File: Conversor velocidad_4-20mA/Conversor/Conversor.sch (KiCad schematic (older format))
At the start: 24 parts, among them J1 Bornera Señal de Entrada, J2 Bornera continua > 15V, J3 BNC salida, Q1 BC848, U1 L7815, U2 4040, U3 4070, U4 TL082

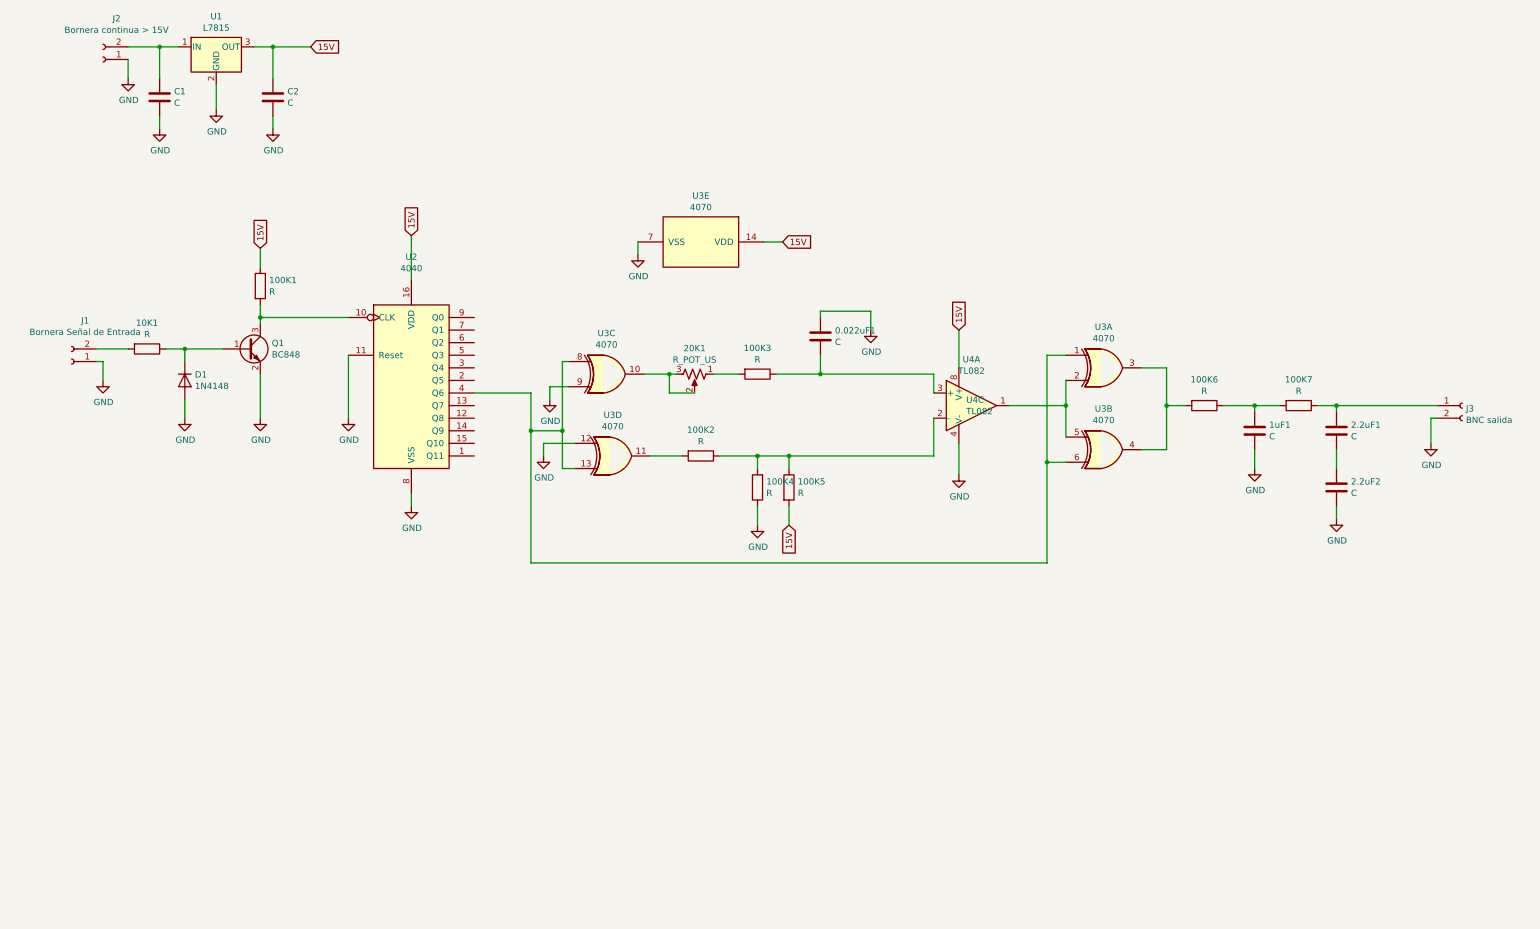
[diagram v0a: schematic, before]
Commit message: Esquemático final
Esquematico final con salida de 4-20mA
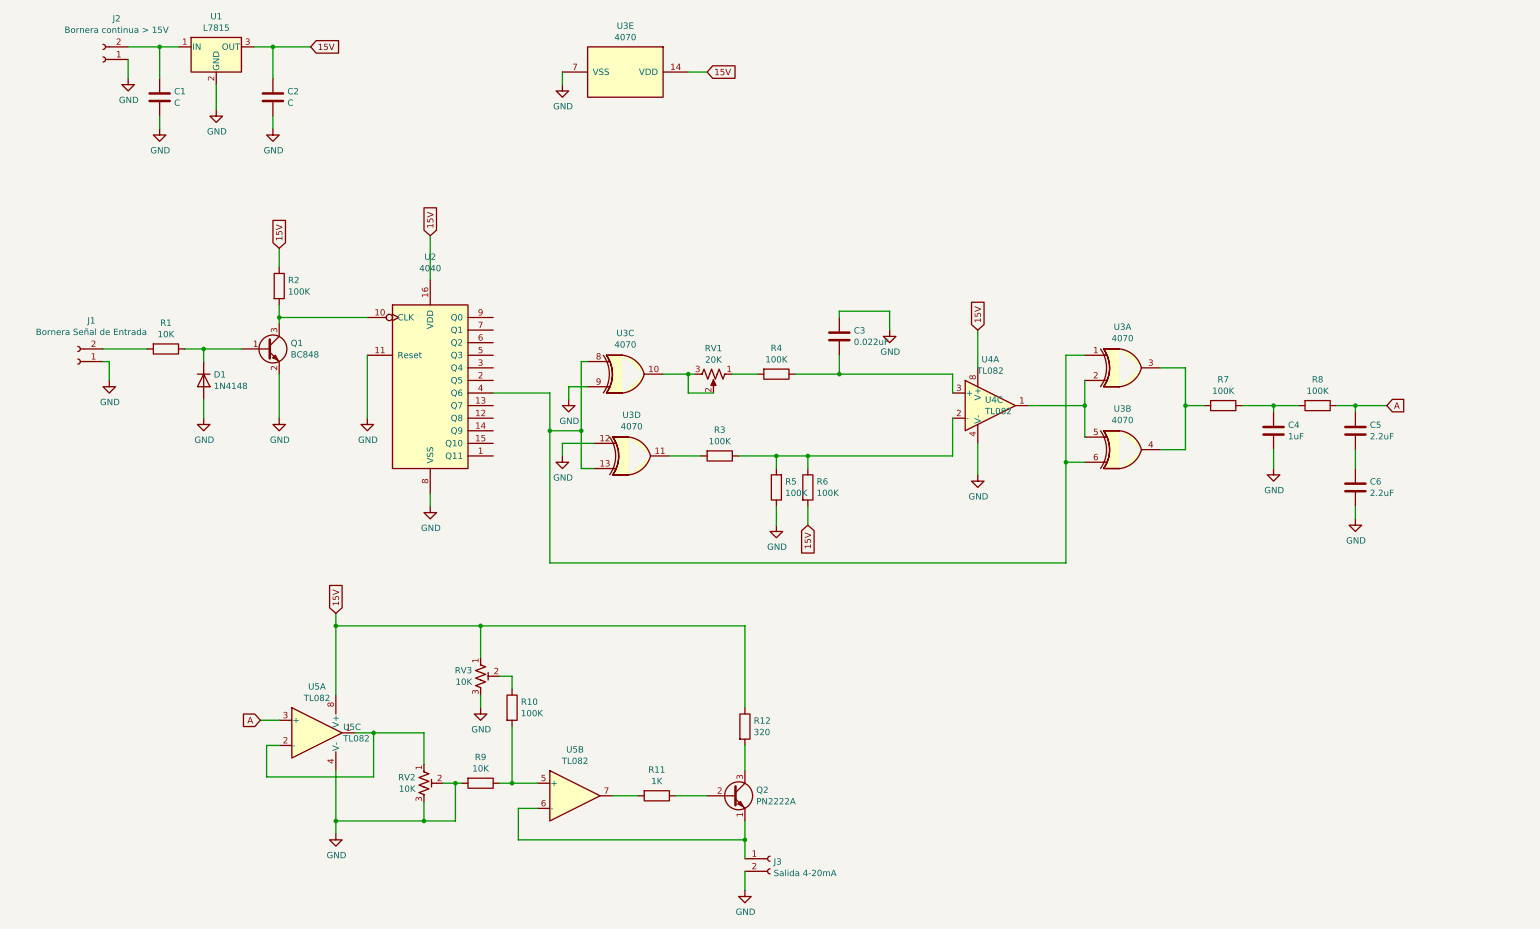
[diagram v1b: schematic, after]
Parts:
- added Q2: PN2222A, Package_TO_SOT_THT:TO-92_Inline, symbol Transistor_BJT:PN2222A
- added R10: 100K, symbol Device:R
- added R11: 1K, symbol Device:R
- added R12: 320, symbol Device:R
- added R9: 10K, symbol Device:R
- added RV2, RV3: 10K, symbol Device:R_POT_TRIM_US
- added U5: TL082, symbol Amplifier_Operational:TL082
- C3: renamed from 0.022uF1; value C -> 0.022uF
- C4: renamed from 1uF1; value C -> 1uF
- C5: renamed from 2.2uF1; value C -> 2.2uF
- C6: renamed from 2.2uF2; value C -> 2.2uF
- J3: value BNC salida -> Salida 4-20mA
- R1: renamed from 10K1; value R -> 10K
- R2: renamed from 100K1; value R -> 100K
- R3: renamed from 100K2; value R -> 100K
- R4: renamed from 100K3; value R -> 100K
- R5: renamed from 100K4; value R -> 100K
- R6: renamed from 100K5; value R -> 100K
- R7: renamed from 100K6; value R -> 100K
- R8: renamed from 100K7; value R -> 100K
- RV1: renamed from 20K1; value R_POT_US -> 20K
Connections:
- net 15V: now also R12.1, RV3.1, U5.8 (V+)
- net GND: now also R9.2, RV2.2, RV2.3, RV3.3, U5.4 (V-)
- net A: now reaches C5.1, R8.1
- net A: now also U5.3 (+); no longer J3.1 (Pin_1)
- new net: RV2.1, U5.1, U5.2 (-)
- new net: R10.2, R9.1, U5.5 (+)
- new net: J3.1 (Pin_1), Q2.1 (E), U5.6 (-)
- new net: R11.2, U5.7
- new net: R10.1, RV3.2
- new net: Q2.2 (B), R11.1
- new net: Q2.3 (C), R12.2
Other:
- moved on the sheet: C3, C4, C5, C6, D1, J1, Q1, R1, R2, R3, R4, R5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
